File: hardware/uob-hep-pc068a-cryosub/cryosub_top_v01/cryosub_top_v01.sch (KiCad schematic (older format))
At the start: 9 parts, among them J1 Conn_02x05_Top_Bottom, J2 Conn_01x04_Male, U1 CMOD-A7

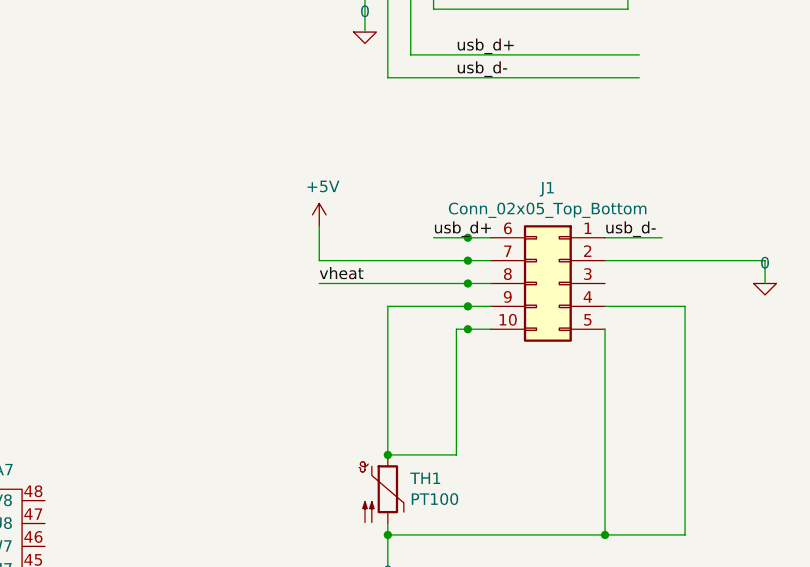
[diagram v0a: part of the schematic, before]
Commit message: Tuning simulation to change on/off temperature. Then making the resulting changes to BoM
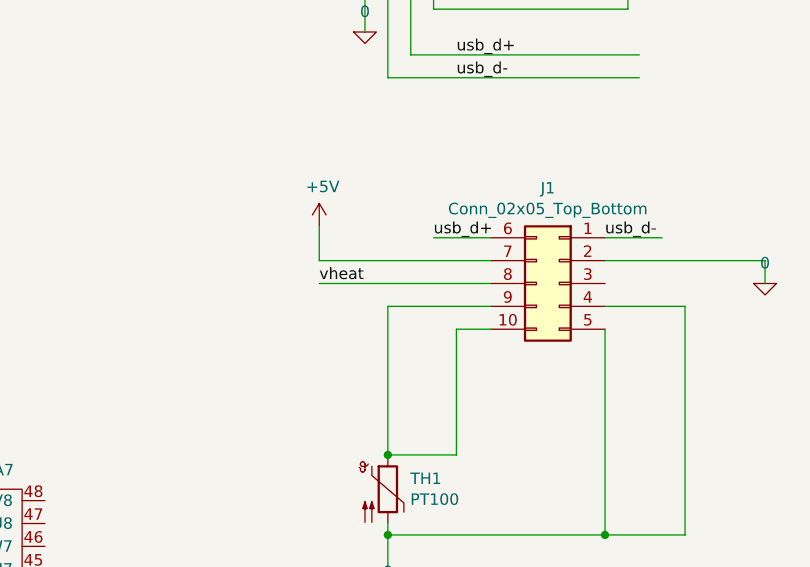
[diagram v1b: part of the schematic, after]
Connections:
- wire segments 56 -> 51
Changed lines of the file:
@@
 *either* fit R23,\n*or* provide power on USB
 Wire Wire Line
-	8950 2200 8850 2200
-Wire Wire Line
 	9450 2200 9700 2200
-Wire Wire Line
-	8950 2300 8850 2300
 Wire Wire Line
 	8200 2300 8200 2150
@@
 Wire Wire Line
 	10150 2300 10150 2400
-Wire Wire Line
-	8950 2400 8850 2400
 Text Label 8800 1400 0    50   ~ 0
 usb_d+
@@
 	9450 3500 9800 3500
 Wire Wire Line
-	8800 2600 8850 2600
-Wire Wire Line
 	8800 2600 8800 3150
-Wire Wire Line
-	8500 2500 8850 2500
 Wire Wire Line
 	8500 2500 8500 3150
@@
 	-1   0    0    -1
 $EndComp
-Connection ~ 8850 2600
 Wire Wire Line
-	8850 2600 8950 2600
-Connection ~ 8850 2200
+	8700 2200 8950 2200
 Wire Wire Line
-	8850 2200 8700 2200
-Connection ~ 8850 2300
+	8200 2300 8950 2300
 Wire Wire Line
-	8850 2300 8200 2300
-Connection ~ 8850 2400
+	8200 2400 8950 2400
 Wire Wire Line
-	8850 2400 8200 2400
-Connection ~ 8850 2500
+	8800 2600 8950 2600
 Wire Wire Line
-	8850 2500 8950 2500
+	8500 2500 8950 2500
 $EndSCHEMATC
